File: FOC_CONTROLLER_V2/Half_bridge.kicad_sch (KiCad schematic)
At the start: 8 parts, among them Q1 CSD18502Q5B, Q3 CSD18502Q5B

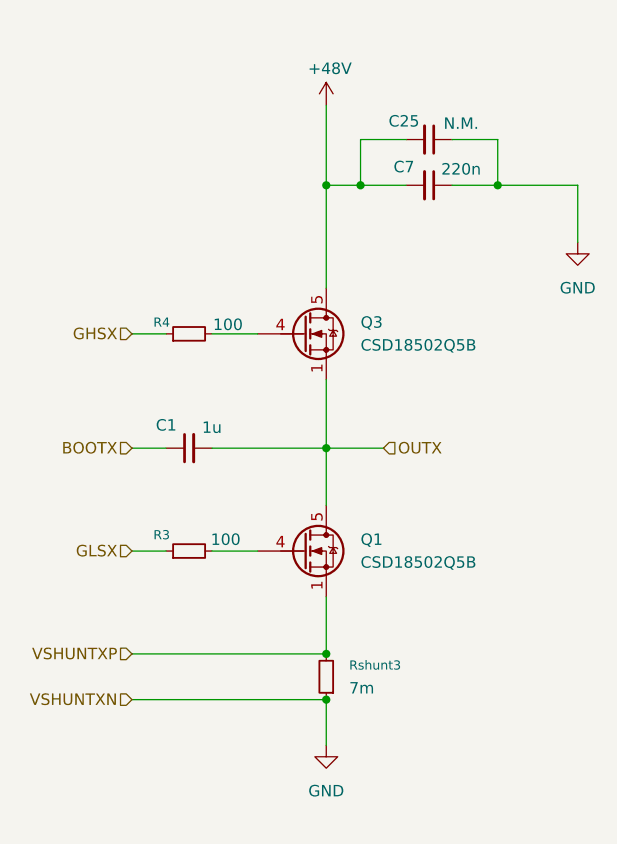
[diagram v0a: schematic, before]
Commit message: Routage Phases PCB
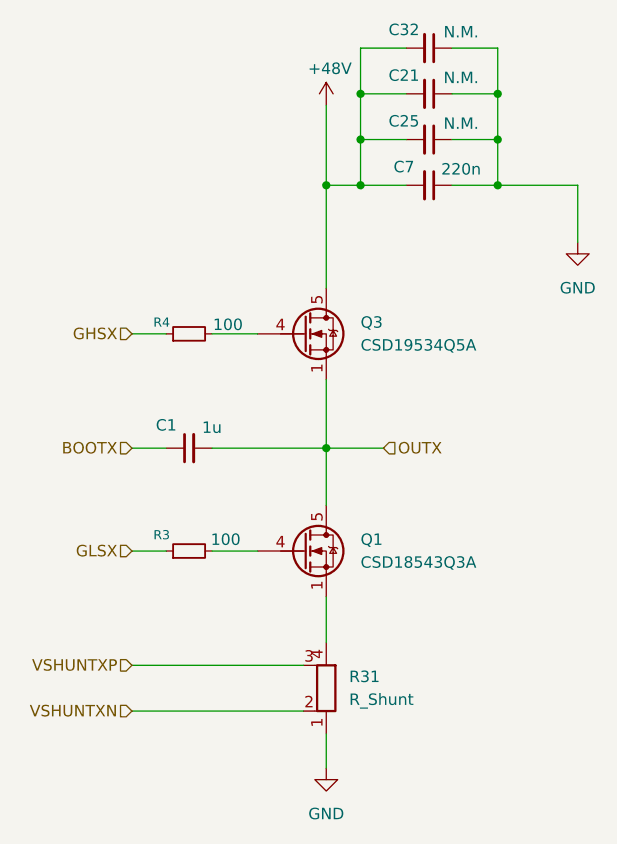
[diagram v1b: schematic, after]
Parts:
- removed Rshunt3: 7m, Resistor_SMD:R_2512_6332Metric_Pad1.40x3.35mm_HandSolder, symbol Device:R_Small
- added C21, C32: N.M., Capacitor_SMD:C_1210_3225Metric_Pad1.33x2.70mm_HandSolder, symbol Device:C_Small
- added R31: R_Shunt, shunt:R_2512_6332Metric_Pad1.40x3.35mm_HandSolder, symbol Device:R_Shunt
- C1: footprint Capacitor_SMD:C_1206_3216Metric -> Capacitor_SMD:C_0805_2012Metric
- C25, C7: footprint Capacitor_SMD:C_1206_3216Metric_Pad1.33x1.80mm_HandSolder -> Capacitor_SMD:C_1210_3225Metric_Pad1.33x2.70mm_HandSolder
- Q1: value CSD18502Q5B -> CSD18543Q3A
- Q3: value CSD18502Q5B -> CSD19534Q5A
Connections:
- net +48V: now also C21.2, C32.2
- net GND: now also C21.1, C32.1, R31.1
- net VSHUNTXP: now also R31.3; no longer Q1.1 (S), Q1.2 (S), Q1.3 (S)
- new net: Q1.1 (S), Q1.2 (S), Q1.3 (S), R31.4
- new net VSHUNTXN: R31.2

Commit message: PCB driver : DONE
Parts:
- R3, R4: footprint Capacitor_SMD:C_0603_1608Metric -> Resistor_SMD:R_0603_1608Metric
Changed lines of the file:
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@@
 			)
 		)
-		(property "Footprint" "Capacitor_SMD:C_0603_1608Metric"
+		(property "Footprint" "Resistor_SMD:R_0603_1608Metric"
 			(at 59.69 101.6 0)
 			(effects
@@
 			)
 		)
-		(property "Footprint" "Capacitor_SMD:C_0603_1608Metric"
+		(property "Footprint" "Resistor_SMD:R_0603_1608Metric"
 			(at 59.69 77.47 0)
 			(effects
